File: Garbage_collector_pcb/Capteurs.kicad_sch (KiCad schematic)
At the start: 6 parts, among them J10 Conn_APDS, J7 Conn_TOF1, J8 Conn_TOF2, J9 Conn_TOF3

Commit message: seance 24 septembre
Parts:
- removed J10: Conn_APDS, Connector_JST:JST_EH_S6B-EH_1x06_P2.50mm_Horizontal, symbol Connector:Conn_01x06_Pin
- removed J7: Conn_TOF1, Connector_JST:JST_EH_S6B-EH_1x06_P2.50mm_Horizontal, symbol Connector:Conn_01x06_Pin
- removed J8: Conn_TOF2, Connector_JST:JST_EH_S6B-EH_1x06_P2.50mm_Horizontal, symbol Connector:Conn_01x06_Pin
- removed J9: Conn_TOF3, Connector_JST:JST_EH_S6B-EH_1x06_P2.50mm_Horizontal, symbol Connector:Conn_01x06_Pin
- added J4: TOF1, symbol Kicad:Conn_01x06
- added J5: TOF3, symbol Kicad:Conn_01x06
- added J6: TOF+Couleur, symbol Kicad:Conn_01x06
- added J7: TOF2, symbol Kicad:Conn_01x06
- added J8: NeoPixel, symbol Kicad:Conn_01x04
- added J9: Lidar, symbol Kicad:Conn_01x04
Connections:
- net +3.3V: now also J4.1 (Pin_1), J5.1 (Pin_1), J6.1 (Pin_1), J7.1 (Pin_1)
- net APDS_INT: now also J6.6 (Pin_6)
- net GND: now also J4.2 (Pin_2), J5.2 (Pin_2), J6.3 (Pin_3), J7.2 (Pin_2), J8.4 (Pin_4), J9.3 (Pin_3)
- net I2C1_SCL: now also R6.2, J4.3 (Pin_3), J5.3 (Pin_3), J6.4 (Pin_4), J7.3 (Pin_3); no longer R5.2
- net I2C1_SDA: now also R5.2, J4.4 (Pin_4), J5.4 (Pin_4), J6.5 (Pin_5), J7.4 (Pin_4); no longer R6.2
- net TOF1_GPIO1: now also J4.5 (Pin_5)
- net TOF1_XST: now also J4.6 (Pin_6)
- net TOF2_GPIO1: now also J7.5 (Pin_5)
- net TOF2_XST: now also J7.6 (Pin_6)
- net TOF3_GPIO1: now also J5.5 (Pin_5)
- net TOF3_XST: now also J5.6 (Pin_6)
- new net +5V: J8.1 (Pin_1), J9.1 (Pin_1)
- new net Lidar_M_CTR: J9.4 (Pin_4)
- new net Lidar_Tx: J9.2 (Pin_2)
- new net Neo_Din: J8.2 (Pin_2)
- new net Neo_Dout: J8.3 (Pin_3)

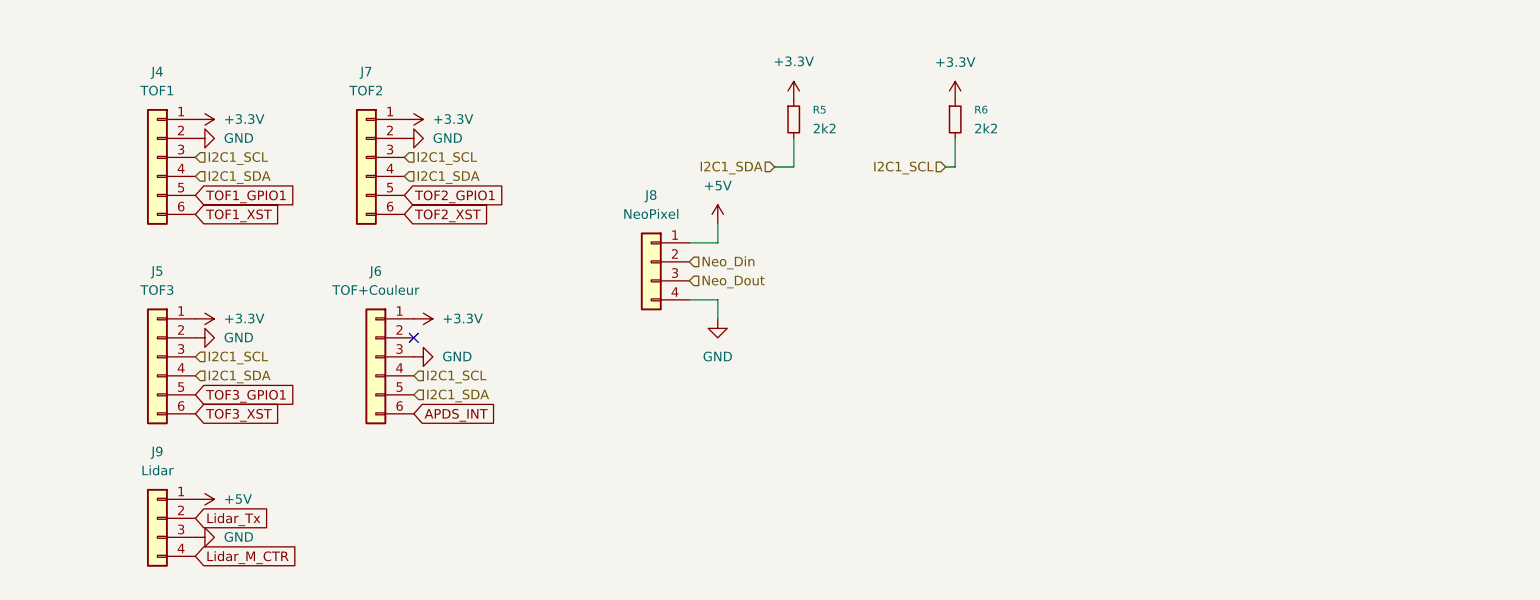
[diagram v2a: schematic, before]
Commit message: update MCU+Moteurs+Capteurs parts + assignement des labels + assignement des pins sur l'ioc (CubeMX)
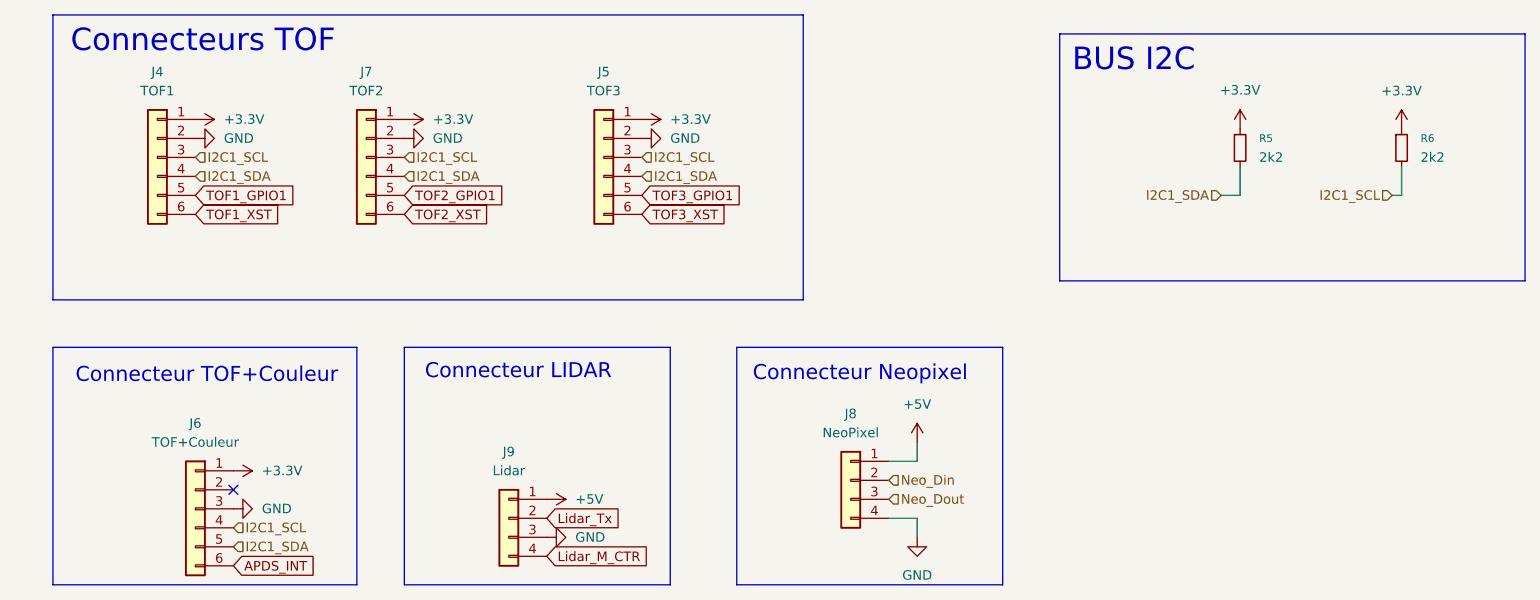
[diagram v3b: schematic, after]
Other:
- note added: "BUS I2C"
- note added: "Connecteur LIDAR"
- note added: "Connecteur Neopixel"
- note added: "Connecteur TOF+Couleur"
- note added: "Connecteurs TOF"
- moved on the sheet: J5, J6, J8, J9, R5, R6

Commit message: update schematic
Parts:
- renumbered J7 to J10, J9 to J11, J5 to J12, J8 to J13, J4 to J8, J6 to J9, R5 to R30, R6 to R31
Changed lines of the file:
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@@
 		(dnp no)
 		(fields_autoplaced yes)
-		(property "Reference" "J8"
+		(property "Reference" "J13"
 			(at 134.62 72.39 0)
 			(show_name no)
@@
 			(project "Garbage_collector"
 				(path "/158d6e2c-2f49-4796-8b5c-460e7c4b776f/1cd51e4b-643c-4b3d-a928-ed2f20ca0ace"
-					(reference "J8")
+					(reference "J13")
 					(unit 1)
 				)
@@
 		(dnp no)
 		(fields_autoplaced yes)
-		(property "Reference" "J4"
+		(property "Reference" "J8"
 			(at 41.91 26.67 0)
 			(show_name no)
@@
 			(project "Garbage_collector"
 				(path "/158d6e2c-2f49-4796-8b5c-460e7c4b776f/1cd51e4b-643c-4b3d-a928-ed2f20ca0ace"
-					(reference "J4")
+					(reference "J8")
 					(unit 1)
 				)
@@
 		(dnp no)
 		(fields_autoplaced yes)
-		(property "Reference" "#PWR034"
+		(property "Reference" "#PWR081"
 			(at 186.69 38.1 0)
 			(hide yes)
@@
 			(project "Garbage_collector"
 				(path "/158d6e2c-2f49-4796-8b5c-460e7c4b776f/1cd51e4b-643c-4b3d-a928-ed2f20ca0ace"
-					(reference "#PWR034")
+					(reference "#PWR081")
 					(unit 1)
 				)
@@
 		(dnp no)
 		(fields_autoplaced yes)
-		(property "Reference" "#PWR026"
+		(property "Reference" "#PWR069"
 			(at 43.18 33.02 0)
 			(hide yes)
@@
 			(project "Garbage_collector"
 				(path "/158d6e2c-2f49-4796-8b5c-460e7c4b776f/1cd51e4b-643c-4b3d-a928-ed2f20ca0ace"
-					(reference "#PWR026")
+					(reference "#PWR069")
 					(unit 1)
 				)
@@
 		(dnp no)
 		(fields_autoplaced yes)
-		(property "Reference" "#PWR010"
+		(property "Reference" "#PWR076"
 			(at 100.33 88.9 0)
 			(hide yes)
@@
 			(project "Garbage_collector"
 				(path "/158d6e2c-2f49-4796-8b5c-460e7c4b776f/1cd51e4b-643c-4b3d-a928-ed2f20ca0ace"
-					(reference "#PWR010")
+					(reference "#PWR076")
 					(unit 1)
 				)
@@
 		(dnp no)
 		(fields_autoplaced yes)
-		(property "Reference" "#PWR033"
+		(property "Reference" "#PWR072"
 			(at 58.42 85.09 0)
 			(hide yes)
@@
 			(project "Garbage_collector"
 				(path "/158d6e2c-2f49-4796-8b5c-460e7c4b776f/1cd51e4b-643c-4b3d-a928-ed2f20ca0ace"
-					(reference "#PWR033")
+					(reference "#PWR072")
 					(unit 1)
 				)
@@
 		(dnp no)
 		(fields_autoplaced yes)
-		(property "Reference" "R5"
+		(property "Reference" "R30"
 			(at 189.23 35.5599 0)
 			(show_name no)
@@
 			(project "Garbage_collector"
 				(path "/158d6e2c-2f49-4796-8b5c-460e7c4b776f/1cd51e4b-643c-4b3d-a928-ed2f20ca0ace"
-					(reference "R5")
+					(reference "R30")
 					(unit 1)
 				)
@@
 		(dnp no)
 		(fields_autoplaced yes)
-		(property "Reference" "#PWR029"
+		(property "Reference" "#PWR070"
 			(at 53.34 35.56 0)
 			(hide yes)
@@
 			(project "Garbage_collector"
 				(path "/158d6e2c-2f49-4796-8b5c-460e7c4b776f/1cd51e4b-643c-4b3d-a928-ed2f20ca0ace"
-					(reference "#PWR029")
+					(reference "#PWR070")
 					(unit 1)
 				)
@@
 		(dnp no)
 		(fields_autoplaced yes)
-		(property "Reference" "J5"
+		(property "Reference" "J12"
 			(at 101.6 26.67 0)
 			(show_name no)
@@
 			(project "Garbage_collector"
 				(path "/158d6e2c-2f49-4796-8b5c-460e7c4b776f/1cd51e4b-643c-4b3d-a928-ed2f20ca0ace"
-					(reference "J5")
+					(reference "J12")
 					(unit 1)
 				)
@@
 		(dnp no)
 		(fields_autoplaced yes)
-		(property "Reference" "#PWR069"
+		(property "Reference" "#PWR080"
 			(at 143.51 95.25 0)
 			(hide yes)
@@
 			(project "Garbage_collector"
 				(path "/158d6e2c-2f49-4796-8b5c-460e7c4b776f/1cd51e4b-643c-4b3d-a928-ed2f20ca0ace"
-					(reference "#PWR069")
+					(reference "#PWR080")
 					(unit 1)
 				)
@@
 		(dnp no)
 		(fields_autoplaced yes)
-		(property "Reference" "#PWR031"
+		(property "Reference" "#PWR078"
 			(at 113.03 35.56 0)
 			(hide yes)
@@
 			(project "Garbage_collector"
 				(path "/158d6e2c-2f49-4796-8b5c-460e7c4b776f/1cd51e4b-643c-4b3d-a928-ed2f20ca0ace"
-					(reference "#PWR031")
+					(reference "#PWR078")
 					(unit 1)
 				)
@@
 		(dnp no)
 		(fields_autoplaced yes)
-		(property "Reference" "#PWR030"
+		(property "Reference" "#PWR074"
 			(at 81.28 35.56 0)
 			(hide yes)
@@
 			(project "Garbage_collector"
 				(path "/158d6e2c-2f49-4796-8b5c-460e7c4b776f/1cd51e4b-643c-4b3d-a928-ed2f20ca0ace"
-					(reference "#PWR030")
+					(reference "#PWR074")
 					(unit 1)
 				)
@@
 		(dnp no)
 		(fields_autoplaced yes)
-		(property "Reference" "#PWR027"
+		(property "Reference" "#PWR077"
 			(at 102.87 33.02 0)
 			(hide yes)
@@
 			(project "Garbage_collector"
 				(path "/158d6e2c-2f49-4796-8b5c-460e7c4b776f/1cd51e4b-643c-4b3d-a928-ed2f20ca0ace"
-					(reference "#PWR027")
+					(reference "#PWR077")
 					(unit 1)
 				)
@@
 		(dnp no)
 		(fields_autoplaced yes)
-		(property "Reference" "#PWR032"
+		(property "Reference" "#PWR071"
 			(at 48.26 80.01 0)
 			(hide yes)
@@
 			(project "Garbage_collector"
 				(path "/158d6e2c-2f49-4796-8b5c-460e7c4b776f/1cd51e4b-643c-4b3d-a928-ed2f20ca0ace"
-					(reference "#PWR032")
+					(reference "#PWR071")
 					(unit 1)
 				)
@@
 		(dnp no)
 		(fields_autoplaced yes)
-		(property "Reference" "J7"
+		(property "Reference" "J10"
 			(at 69.85 26.67 0)
 			(show_name no)
@@
 			(project "Garbage_collector"
 				(path "/158d6e2c-2f49-4796-8b5c-460e7c4b776f/1cd51e4b-643c-4b3d-a928-ed2f20ca0ace"
-					(reference "J7")
+					(reference "J10")
 					(unit 1)
 				)
@@
 		(dnp no)
 		(fields_autoplaced yes)
-		(property "Reference" "#PWR035"
+		(property "Reference" "#PWR082"
 			(at 208.28 38.1 0)
 			(hide yes)
@@
 			(project "Garbage_collector"
 				(path "/158d6e2c-2f49-4796-8b5c-460e7c4b776f/1cd51e4b-643c-4b3d-a928-ed2f20ca0ace"
-					(reference "#PWR035")
+					(reference "#PWR082")
 					(unit 1)
 				)
@@
 		(dnp no)
 		(fields_autoplaced yes)
-		(property "Reference" "R6"
+		(property "Reference" "R31"
 			(at 210.82 35.5599 0)
 			(show_name no)
@@
 			(project "Garbage_collector"
 				(path "/158d6e2c-2f49-4796-8b5c-460e7c4b776f/1cd51e4b-643c-4b3d-a928-ed2f20ca0ace"
-					(reference "R6")
+					(reference "R31")
 					(unit 1)
 				)
@@
 		(dnp no)
 		(fields_autoplaced yes)
-		(property "Reference" "#PWR09"
+		(property "Reference" "#PWR075"
 			(at 90.17 83.82 0)
 			(hide yes)
@@
 			(project "Garbage_collector"
 				(path "/158d6e2c-2f49-4796-8b5c-460e7c4b776f/1cd51e4b-643c-4b3d-a928-ed2f20ca0ace"
-					(reference "#PWR09")
+					(reference "#PWR075")
 					(unit 1)
 				)
@@
 		(dnp no)
 		(fields_autoplaced yes)
-		(property "Reference" "J6"
+		(property "Reference" "J9"
 			(at 46.99 73.66 0)
 			(show_name no)
@@
 			(project "Garbage_collector"
 				(path "/158d6e2c-2f49-4796-8b5c-460e7c4b776f/1cd51e4b-643c-4b3d-a928-ed2f20ca0ace"
-					(reference "J6")
+					(reference "J9")
 					(unit 1)
 				)
@@
 		(dnp no)
 		(fields_autoplaced yes)
-		(property "Reference" "J9"
+		(property "Reference" "J11"
 			(at 88.9 77.47 0)
 			(show_name no)
@@
 			(project "Garbage_collector"
 				(path "/158d6e2c-2f49-4796-8b5c-460e7c4b776f/1cd51e4b-643c-4b3d-a928-ed2f20ca0ace"
-					(reference "J9")
+					(reference "J11")
 					(unit 1)
 				)
@@
 		(dnp no)
 		(fields_autoplaced yes)
-		(property "Reference" "#PWR08"
+		(property "Reference" "#PWR079"
 			(at 143.51 80.01 0)
 			(hide yes)
@@
 			(project "Garbage_collector"
 				(path "/158d6e2c-2f49-4796-8b5c-460e7c4b776f/1cd51e4b-643c-4b3d-a928-ed2f20ca0ace"
-					(reference "#PWR08")
+					(reference "#PWR079")
 					(unit 1)
 				)
@@
 		(dnp no)
 		(fields_autoplaced yes)
-		(property "Reference" "#PWR028"
+		(property "Reference" "#PWR073"
 			(at 71.12 33.02 0)
 			(hide yes)
@@
 			(project "Garbage_collector"
 				(path "/158d6e2c-2f49-4796-8b5c-460e7c4b776f/1cd51e4b-643c-4b3d-a928-ed2f20ca0ace"
-					(reference "#PWR028")
-					(unit 1)
-				)
+					(reference "#PWR073")
+					(unit 1)
+				)

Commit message: ajout du ioc et schema validé
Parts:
- removed J10: TOF2, symbol Kicad:Conn_01x06
- removed J12: TOF3, symbol Kicad:Conn_01x06
- removed J13: NeoPixel, symbol Kicad:Conn_01x04
- removed J8: TOF1, symbol Kicad:Conn_01x06
- removed J9: TOF+Couleur, symbol Kicad:Conn_01x06
- added C31, C41, C42, C43, C44: 100n, Capacitor_SMD:C_0402_1005Metric, symbol Device:C_Small
- added J4: NEOPIXELS, Connector_JST:JST_GH_SM03B-GHS-TB_1x03-1MP_P1.25mm_Horizontal, symbol Connector_Generic:Conn_01x03
- added J7: ADA3595, Connector_JST:JST_GH_SM05B-GHS-TB_1x05-1MP_P1.25mm_Horizontal, symbol Connector_Generic:Conn_01x05
- added J8, J9: VL53L0CXV0DH1, Connector_JST:JST_GH_SM06B-GHS-TB_1x06-1MP_P1.25mm_Horizontal, symbol Connector_Generic:Conn_01x06
- added R12: 300, Resistor_SMD:R_0603_1608Metric, symbol Device:R_Small
- added U6: SN74AHCT1G125DBVR, Package_TO_SOT_SMD:SOT-23-5, symbol 74xGxx:74AHCT1G125
- J11: footprint (none) -> Connector_JST:JST_GH_BM04B-GHS-TBT_1x04-1MP_P1.25mm_Vertical
- R30, R31: JLCPCB Part # (none) -> C25879; now not fitted
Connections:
- net +3.3V: now also C42.1, C43.1, C44.1, J7.5 (Pin_5), J8.6 (Pin_6), J9.6 (Pin_6)
- net +5V: now also C31.1, C41.1, J4.3 (Pin_3), U6.5 (VCC)
- net GND: now also C31.2, C41.2, C42.2, C43.2, C44.2, J4.1 (Pin_1), J7.4 (Pin_4), J8.5 (Pin_5), J9.5 (Pin_5), U6.1, U6.3 (GND)
- net I2C1_SCL: now also J7.3 (Pin_3), J8.4 (Pin_4), J9.4 (Pin_4)
- net I2C1_SDA: now also J7.2 (Pin_2), J8.3 (Pin_3), J9.3 (Pin_3)
- net Neo_Din: now also U6.2
- net TOF1_XST: now also J8.1 (Pin_1)
- net TOF2_XST: now also J9.1 (Pin_1)
- net Lidar_M_CTR renamed Lidar_M_CTRL
- net Lidar_Tx renamed Lidar_TX
- new net: J4.2 (Pin_2), R12.1
- new net: R12.2, U6.4
- new net COLOR_INT: J7.1 (Pin_1)
- new net TOF1_INT: J8.2 (Pin_2)
- new net TOF2_INT: J9.2 (Pin_2)
- no-connect marks 1 -> 0
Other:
- note added: "Connecteur Couleur"
- note removed: "Connecteur TOF+Couleur"
- moved on the sheet: J11

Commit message: ajout des codes pour le nrf52840
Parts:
- R30, R31: footprint Resistor_SMD:R_01005_0402Metric -> Resistor_SMD:R_0603_1608Metric_Pad0.98x0.95mm_HandSolder
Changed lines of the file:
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@@
 			)
 		)
-		(property "Footprint" "Resistor_SMD:R_01005_0402Metric"
+		(property "Footprint" "Resistor_SMD:R_0603_1608Metric_Pad0.98x0.95mm_HandSolder"
 			(at 144.78 34.29 0)
 			(hide yes)
@@
 			)
 		)
-		(property "Footprint" "Resistor_SMD:R_01005_0402Metric"
+		(property "Footprint" "Resistor_SMD:R_0603_1608Metric_Pad0.98x0.95mm_HandSolder"
 			(at 123.19 34.29 0)
 			(hide yes)

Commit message: finalisation des empreintes
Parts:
- J9: renamed from J7; footprint Connector_JST:JST_GH_SM05B-GHS-TB_1x05-1MP_P1.25mm_Horizontal -> Connector_JST:JST_GH_SM06B-GHS-TB_1x06-1MP_P1.25mm_Horizontal
- renumbered C43 to C35, C42 to C36, C44 to C37, C41 to C38, C31 to C39, J11 to J10, J9 to J11, J4 to J12, R30 to R27, R31 to R28, R12 to R29, U6 to U5

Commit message: routage du pcb quasiment terminé, 1 erreur DRC
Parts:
- J9: footprint Connector_JST:JST_GH_SM06B-GHS-TB_1x06-1MP_P1.25mm_Horizontal -> Connector_JST:JST_GH_BM05B-GHS-TBT_1x05-1MP_P1.25mm_Vertical
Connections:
- net +3.3V: now also J9.1 (Pin_1); no longer J9.5 (Pin_5)
- net COLOR_INT: now also J9.5 (Pin_5); no longer J9.1 (Pin_1)
- net GND: now also J9.2 (Pin_2); no longer J9.4 (Pin_4)
- net I2C1_SDA: now also J9.4 (Pin_4); no longer J9.2 (Pin_2)
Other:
- moved on the sheet: J9
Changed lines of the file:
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@@
 	(symbol
 		(lib_id "Connector_Generic:Conn_01x05")
-		(at 34.29 83.82 180)
+		(at 34.29 83.82 0)
+		(mirror y)
 		(unit 1)
 		(body_style 1)
@@
 		(in_pos_files yes)
 		(dnp no)
-		(fields_autoplaced yes)
 		(property "Reference" "J9"
-			(at 34.29 72.39 0)
+			(at 34.29 75.184 0)
 			(show_name no)
 			(do_not_autoplace no)
@@
 		)
 		(property "Value" "ADA3595"
-			(at 34.29 74.93 0)
+			(at 35.052 72.644 0)
 			(show_name no)
 			(do_not_autoplace no)
@@
 			)
 		)
-		(property "Footprint" "Connector_JST:JST_GH_SM06B-GHS-TB_1x06-1MP_P1.25mm_Horizontal"
+		(property "Footprint" "Connector_JST:JST_GH_BM05B-GHS-TBT_1x05-1MP_P1.25mm_Vertical"
 			(at 34.29 83.82 0)
 			(hide yes)
